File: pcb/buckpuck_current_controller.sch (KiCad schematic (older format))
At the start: 10 parts, among them K1 CCB, P1 POWER, SW1 SPST

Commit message: Added some components to the schematic
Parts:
- added BP? (x3): BUCKPUCK, symbol BUCKPUCK
- added P? (x4): CONN_2, symbol CONN_2
- added RV? (x3): 5k, symbol POT
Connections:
- net labels added: CtrlA, CtrlB, CtrlC, CtrlD, CurrentSenseA, CurrentSenseB, CurrentSenseC, CurrentSenseD, DisplayRX, DisplayTX, PotentiometerA, PotentiometerB, PotentiometerC, PotentiometerD, PwmA, PwmB, PwmC, PwmD, SwitchA, SwitchB, SwitchC, SwitchD, VCC
- wire segments 23 -> 87
- no-connect marks 0 -> 13
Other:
- moved on the sheet: RV1

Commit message: Added single_buckpuck_channel.sch and some datasheets
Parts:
- removed BP1, BP? (x3): BUCKPUCK, symbol BUCKPUCK
- removed K1: CCB, symbol CONN_3
- removed P? (x4): CONN_2, symbol CONN_2
- removed RV1, RV? (x3): 5k, symbol POT
- removed SW1: SPST, symbol SPST
- removed TP1: CS-, symbol TESTPOINT
- removed TP2: CS+, symbol TESTPOINT
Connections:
- net labels added: OnOffSwitchA, OnOffSwitchB, OnOffSwitchC, OnOffSwitchD
- net labels removed: CtrlA, CtrlB, CtrlC, CtrlD, SwitchA, SwitchB, SwitchC, SwitchD, VCC
- wire segments 87 -> 43
- no-connect marks 13 -> 9

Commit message: Finished schematic design, added new datasheets...
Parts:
- added C?: 0.33uF, symbol C
- added C?: 0.1uF, symbol C
- added C? (x2): 10uF, symbol C
- added P?: CONN_2X2, symbol CONN_2X2
- added P?: Display, symbol CONN_4
- added R?: 68, symbol R
- added SW?: SetSwitch, symbol SPST
- added U?: V7809, symbol V7809
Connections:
- net labels added: +5V, RST, VDD
- wire segments 43 -> 89
- no-connect marks 9 -> 8
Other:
- moved on the sheet: U?

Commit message: Finished netlist, begun laying out board.  Added datasheets.
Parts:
- removed SW?: SetSwitch, symbol SPST
- added P3: SetSwitch, symbol CONN_2
- P2: renamed from P?; value CONN_2X2 -> ResetOverride
- gave numbers to parts that had none: 8
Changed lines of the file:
@@
-EESchema Schematic File Version 2  date Tue 17 May 2011 05:19:53 PM PDT
+EESchema Schematic File Version 2  date Wed 18 May 2011 04:50:05 PM PDT
 LIBS:power
 LIBS:device
@@
 Comment4 ""
 $EndDescr
-Connection ~ 6150 1800
-Wire Wire Line
-	6150 1600 6150 1800
+Wire Wire Line
+	2250 5900 2250 6400
 Connection ~ 4250 1800
 Wire Wire Line
-	4250 1900 4250 1800
+	4250 1800 4250 1900
 Wire Wire Line
 	4250 2300 4250 2450
@@
 Connection ~ 3700 1800
 Wire Wire Line
-	4600 1800 3350 1800
+	3350 1800 4600 1800
 Connection ~ 5450 3900
 Wire Wire Line
@@
 	4450 2950 4450 3600
 Wire Wire Line
-	2250 6200 2250 6400
-Wire Wire Line
 	4300 6100 3800 6100
 Wire Wire Line
@@
 	1650 2900 3450 2900
 Wire Wire Line
-	3450 1500 3450 1900
+	3450 1900 3450 1500
 Wire Wire Line
 	1350 1800 1350 950
@@
 Connection ~ 6600 2950
 Wire Wire Line
-	4600 3600 4600 3800
+	4600 3800 4600 3600
 Connection ~ 4600 3700
 Wire Wire Line
@@
 	4300 6200 3800 6200
 Wire Wire Line
-	2650 5000 2250 5000
-Wire Wire Line
-	2250 5000 2250 5200
-Wire Wire Line
-	5450 3900 5450 3700
+	5450 3700 5450 3900
 Wire Wire Line
 	5750 3250 5750 3400
@@
 	5000 2100 5000 2250
 Wire Wire Line
-	5750 1900 5750 1800
+	5750 1800 5750 1900
 Connection ~ 5750 1800
 Wire Wire Line
@@
 Wire Wire Line
 	6550 1800 6550 1650
-$Comp
-L PWR_FLAG #FLG?
-U 1 1 4DD30F98
-P 6150 1600
-F 0 "#FLG?" H 6150 1870 30  0001 C CNN
-F 1 "PWR_FLAG" H 6150 1830 30  0000 C CNN
-	1    6150 1600
-	1    0    0    -1
-$EndComp
-$Comp
-L VDD #PWR?
+Wire Wire Line
+	2650 5000 2050 5000
+Wire Wire Line
+	2050 5000 2050 5700
+Wire Wire Line
+	2050 5700 2250 5700
+$Comp
+L CONN_2 P3
+U 1 1 4DD40675
+P 2600 5800
+F 0 "P3" V 2550 5800 40  0000 C CNN
+F 1 "SetSwitch" V 2650 5800 40  0000 C CNN
+	1    2600 5800
+	1    0    0    -1
+$EndComp
+$Comp
+L VDD #PWR01
 U 1 1 4DD30F8E
 P 6550 1650
-F 0 "#PWR?" H 6550 1750 30  0001 C CNN
+F 0 "#PWR01" H 6550 1750 30  0001 C CNN
 F 1 "VDD" H 6550 1760 30  0000 C CNN
 	1    6550 1650
@@
 $EndComp
 $Comp
-L GND #PWR?
+L GND #PWR02
 U 1 1 4DD30F78
 P 5750 2450
-F 0 "#PWR?" H 5750 2450 30  0001 C CNN
+F 0 "#PWR02" H 5750 2450 30  0001 C CNN
 F 1 "GND" H 5750 2380 30  0001 C CNN
 	1    5750 2450
@@
 $EndComp
 $Comp
-L GND #PWR?
+L GND #PWR03
 U 1 1 4DD30F74
 P 4250 2450
-F 0 "#PWR?" H 4250 2450 30  0001 C CNN
+F 0 "#PWR03" H 4250 2450 30  0001 C CNN
 F 1 "GND" H 4250 2380 30  0001 C CNN
 	1    4250 2450
@@
 $EndComp
 $Comp
-L C C?
+L C C3
 U 1 1 4DD30F54
 P 5750 2100
-F 0 "C?" H 5800 2200 50  0000 L CNN
+F 0 "C3" H 5800 2200 50  0000 L CNN
 F 1 "10uF" H 5800 2000 50  0000 L CNN
 	1    5750 2100
@@
 $EndComp
 $Comp
-L C C?
+L C C2
 U 1 1 4DD30F51
 P 4250 2100
-F 0 "C?" H 4300 2200 50  0000 L CNN
+F 0 "C2" H 4300 2200 50  0000 L CNN
 F 1 "10uF" H 4300 2000 50  0000 L CNN
 	1    4250 2100
@@
 $EndComp
 $Comp
-L GND #PWR?
+L GND #PWR04
 U 1 1 4DD30F46
 P 5000 2250
-F 0 "#PWR?" H 5000 2250 30  0001 C CNN
+F 0 "#PWR04" H 5000 2250 30  0001 C CNN
 F 1 "GND" H 5000 2180 30  0001 C CNN
 	1    5000 2250
@@
 $EndComp
 $Comp
-L V7809 U?
+L V7809 U1
 U 1 1 4DD30F0E
 P 5000 1850
-F 0 "U?" H 5150 1654 60  0000 C CNN
+F 0 "U1" H 5150 1654 60  0000 C CNN
 F 1 "V7809" H 5000 2050 60  0000 C CNN
 	1    5000 1850
@@
 $EndComp
 $Comp
-L +5V #PWR?
+L +5V #PWR05
 U 1 1 4DD308A2
 P 5750 3250
-F 0 "#PWR?" H 5750 3340 20  0001 C CNN
+F 0 "#PWR05" H 5750 3340 20  0001 C CNN
 F 1 "+5V" H 5750 3340 30  0000 C CNN
 	1    5750 3250
@@
 $EndComp
 $Comp
-L PWR_FLAG #FLG?
+L PWR_FLAG #FLG06
 U 1 1 4DD3088D
 P 5700 3850
-F 0 "#FLG?" H 5700 4120 30  0001 C CNN
+F 0 "#FLG06" H 5700 4120 30  0001 C CNN
 F 1 "PWR_FLAG" H 5700 4080 30  0000 C CNN
 	1    5700 3850
@@
 $EndComp
 $Comp
-L +5V #PWR?
+L +5V #PWR07
 U 1 1 4DD3087D
 P 5450 3700
-F 0 "#PWR?" H 5450 3790 20  0001 C CNN
+F 0 "#PWR07" H 5450 3790 20  0001 C CNN
 F 1 "+5V" H 5450 3790 30  0000 C CNN
 	1    5450 3700
@@
 $EndComp
 $Comp
-L VDD #PWR?
+L VDD #PWR08
 U 1 1 4DD3074D
 P 4450 2950
-F 0 "#PWR?" H 4450 3050 30  0001 C CNN
+F 0 "#PWR08" H 4450 3050 30  0001 C CNN
 F 1 "VDD" H 4450 3060 30  0000 C CNN
 	1    4450 2950
@@
 $EndComp
 $Comp
-L GND #PWR?
+L GND #PWR09
 U 1 1 4DD2FA71
 P 2250 6400
-F 0 "#PWR?" H 2250 6400 30  0001 C CNN
+F 0 "#PWR09" H 2250 6400 30  0001 C CNN
 F 1 "GND" H 2250 6330 30  0001 C CNN
 	1    2250 6400
 	1    0    0    -1
-$EndComp
-$Comp
-L SPST SW?
-U 1 1 4DD2FA66
-P 2250 5700
-F 0 "SW?" H 2250 5800 70  0000 C CNN
-F 1 "SetSwitch" H 2250 5600 70  0000 C CNN
-	1    2250 5700
-	0    1    1    0
 $EndComp
 Text Label 3800 6200 0    60   ~ 0
@@
 DisplayRX
 $Comp
-L GND #PWR?
+L GND #PWR010
 U 1 1 4DD2F8D7
 P 3550 6350
-F 0 "#PWR?" H 3550 6350 30  0001 C CNN
+F 0 "#PWR010" H 3550 6350 30  0001 C CNN
 F 1 "GND" H 3550 6280 30  0001 C CNN
 	1    3550 6350
@@
 $EndComp
 $Comp
-L VDD #PWR?
+L VDD #PWR011
 U 1 1 4DD2F8C8
 P 4100 5750
-F 0 "#PWR?" H 4100 5850 30  0001 C CNN
+F 0 "#PWR011" H 4100 5850 30  0001 C CNN
 F 1 "VDD" H 4100 5860 30  0000 C CNN
 	1    4100 5750
@@
 $EndComp
 $Comp
-L CONN_4 P?
+L CONN_4 P4
 U 1 1 4DD2F842
 P 4650 6050
-F 0 "P?" V 4600 6050 50  0000 C CNN
+F 0 "P4" V 4600 6050 50  0000 C CNN
 F 1 "Display" V 4700 6050 50  0000 C CNN
 	1    4650 6050
@@
 $EndComp
 $Comp
-L C C?
+L C C5
 U 1 1 4DD2F791
 P 4600 3400
-F 0 "C?" H 4650 3500 50  0000 L CNN
+F 0 "C5" H 4650 3500 50  0000 L CNN
 F 1 "0.1uF" H 4650 3300 50  0000 L CNN
 	1    4600 3400
@@
 $EndComp
 $Comp
-L GND #PWR?
+L GND #PWR012
 U 1 1 4DD2F728
 P 4600 3800
-F 0 "#PWR?" H 4600 3800 30  0001 C CNN
+F 0 "#PWR012" H 4600 3800 30  0001 C CNN
 F 1 "GND" H 4600 3730 30  0001 C CNN
 	1    4600 3800
@@
 $EndComp
 $Comp
-L GND #PWR?
+L GND #PWR013
 U 1 1 4DD2F63F
 P 6800 3600
-F 0 "#PWR?" H 6800 3600 30  0001 C CNN
+F 0 "#PWR013" H 6800 3600 30  0001 C CNN
 F 1 "GND" H 6800 3530 30  0001 C CNN
 	1    6800 3600
@@
 $EndComp
 $Comp
-L R R?
+L R R1
 U 1 1 4DD2F567
 P 6150 3400
-F 0 "R?" V 6230 3400 50  0000 C CNN
+F 0 "R1" V 6230 3400 50  0000 C CNN
 F 1 "68" V 6150 3400 50  0000 C CNN
 	1    6150 3400
@@
 $EndComp
 $Comp
-L C C?
+L C C4
 U 1 1 4DD2F558
 P 6800 3250
-F 0 "C?" H 6850 3350 50  0000 L CNN
+F 0 "C4" H 6850 3350 50  0000 L CNN
 F 1 "0.33uF" H 6850 3150 50  0000 L CNN
 	1    6800 3250
@@
 NoConn ~ 5650 3050
 $Comp
-L CONN_2X2 P?
+L CONN_2X2 P2
 U 1 1 4DD2F1DB
 P 6050 3000
-F 0 "P?" H 6050 3150 50  0000 C CNN
-F 1 "CONN_2X2" H 6060 2870 40  0000 C CNN
+F 0 "P2" H 6050 3150 50  0000 C CNN
+F 1 "ResetOverride" H 6060 2870 40  0000 C CNN
 	1    6050 3000
 	1    0    0    -1
@@
 DisplayRX
 $Comp
-L GND #PWR01
+L GND #PWR014
 U 1 1 4DB0D0E3
 P 1550 4000
-F 0 "#PWR01" H 1550 4000 30  0001 C CNN
+F 0 "#PWR014" H 1550 4000 30  0001 C CNN
 F 1 "GND" H 1550 3930 30  0001 C CNN
 	1    1550 4000
@@
 CurrentSenseA
 $Comp
-L VAA #PWR?
+L VAA #PWR1
 U 1 1 4DAF3EF4
 P 3700 1600
-F 0 "#PWR?" H 3700 1660 30  0001 C CNN
+F 0 "#PWR1" H 3700 1660 30  0001 C CNN
 F 1 "VAA" H 3700 1710 30  0000 C CNN
 	1    3700 1600
@@
 $EndComp
 $Comp
-L ARDUINO_NANO U?
+L ARDUINO_NANO U2
 U 1 1 4DAF2A1C
 P 3500 4350
-F 0 "U?" H 3050 5300 60  0000 C CNN
+F 0 "U2" H 3050 5300 60  0000 C CNN
 F 1 "ARDUINO_NANO" H 3500 3500 60  0000 C CNN
 	1    3500 4350
@@
 $EndComp
 $Comp
-L GND #PWR02
+L GND #PWR015
 U 1 1 4B884901
 P 3200 3050
-F 0 "#PWR02" H 3200 3050 30  0001 C CNN
+F 0 "#PWR015" H 3200 3050 30  0001 C CNN
 F 1 "GND" H 3200 2980 30  0001 C CNN
 	1    3200 3050
@@
 $EndComp
 $Comp
-L PWR_FLAG #FLG03
+L PWR_FLAG #FLG016
 U 1 1 4B61DEC3
 P 2950 2750
-F 0 "#FLG03" H 2950 3020 30  0001 C CNN
+F 0 "#FLG016" H 2950 3020 30  0001 C CNN
 F 1 "PWR_FLAG" H 2950 2980 30  0000 C CNN
 	1    2950 2750
@@
 $EndComp
 $Comp
-L PWR_FLAG #FLG04
+L PWR_FLAG #FLG017
 U 1 1 4B61DEA9
 P 2400 750
-F 0 "#FLG04" H 2400 1020 30  0001 C CNN
+F 0 "#FLG017" H 2400 1020 30  0001 C CNN
 F 1 "PWR_FLAG" H 2400 980 30  0000 C CNN
 	1    2400 750
@@
 $EndComp
 $Comp
-L PWR_FLAG #FLG05
+L PWR_FLAG #FLG018
 U 1 1 4B61DE8F
 P 3450 1500
-F 0 "#FLG05" H 3450 1770 30  0001 C CNN
+F 0 "#FLG018" H 3450 1770 30  0001 C CNN
 F 1 "PWR_FLAG" H 3450 1730 30  0000 C CNN
 	1    3450 1500

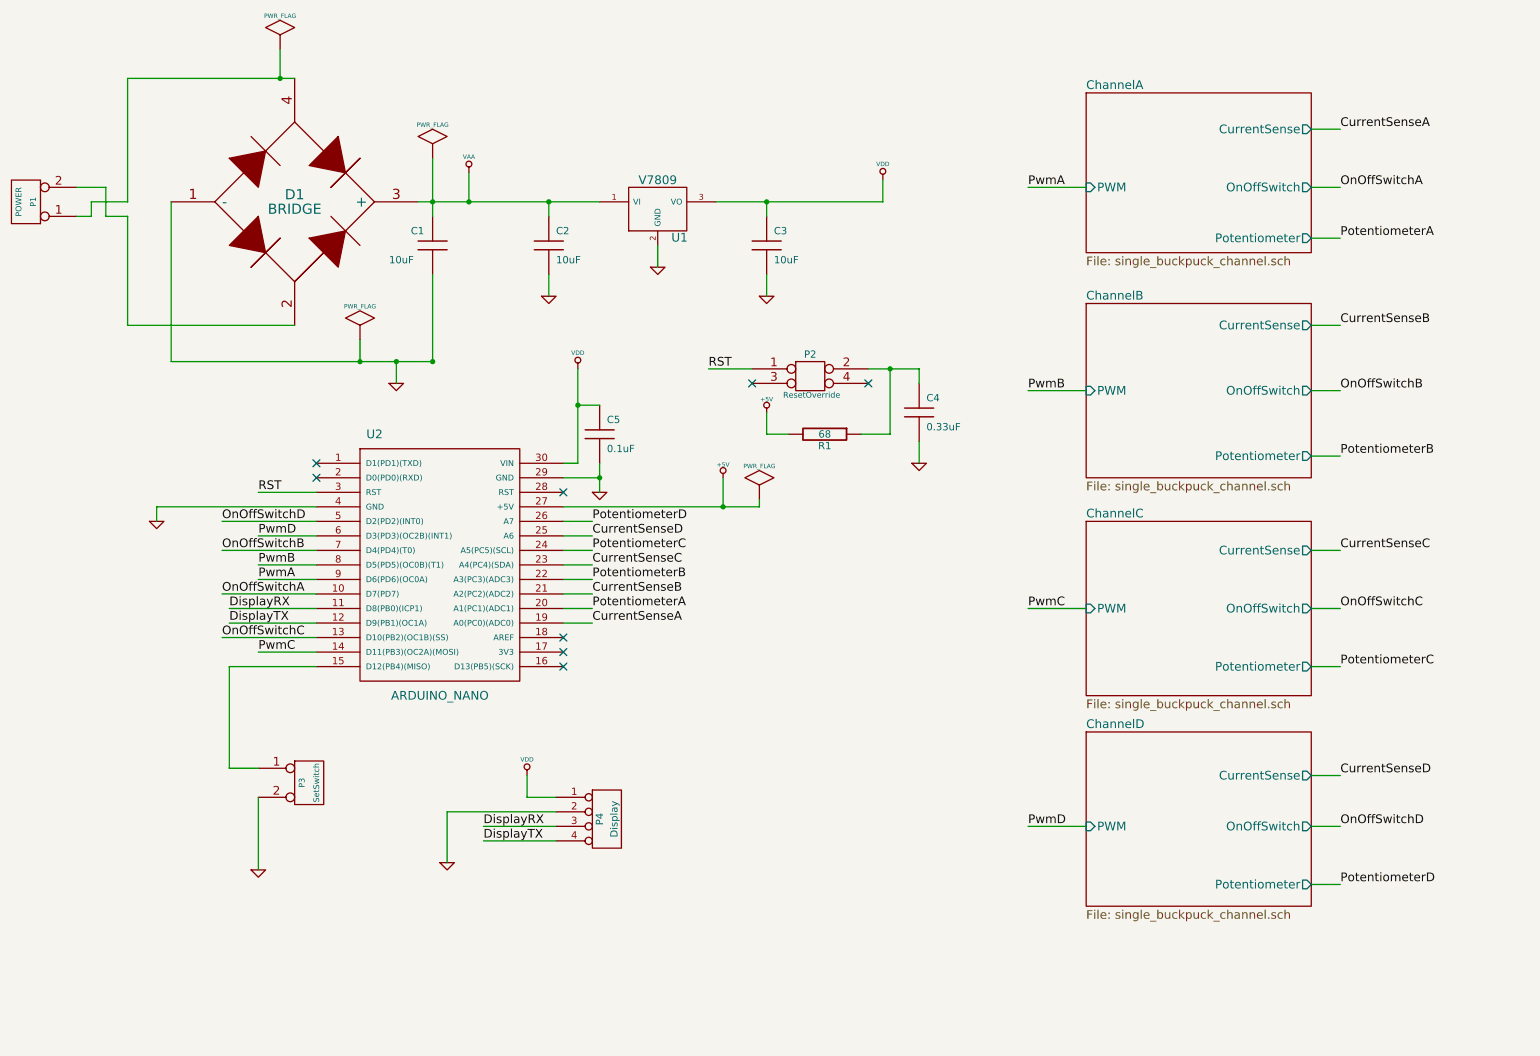
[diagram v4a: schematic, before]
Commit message: Finished routing board.  Examine one more time before being made.
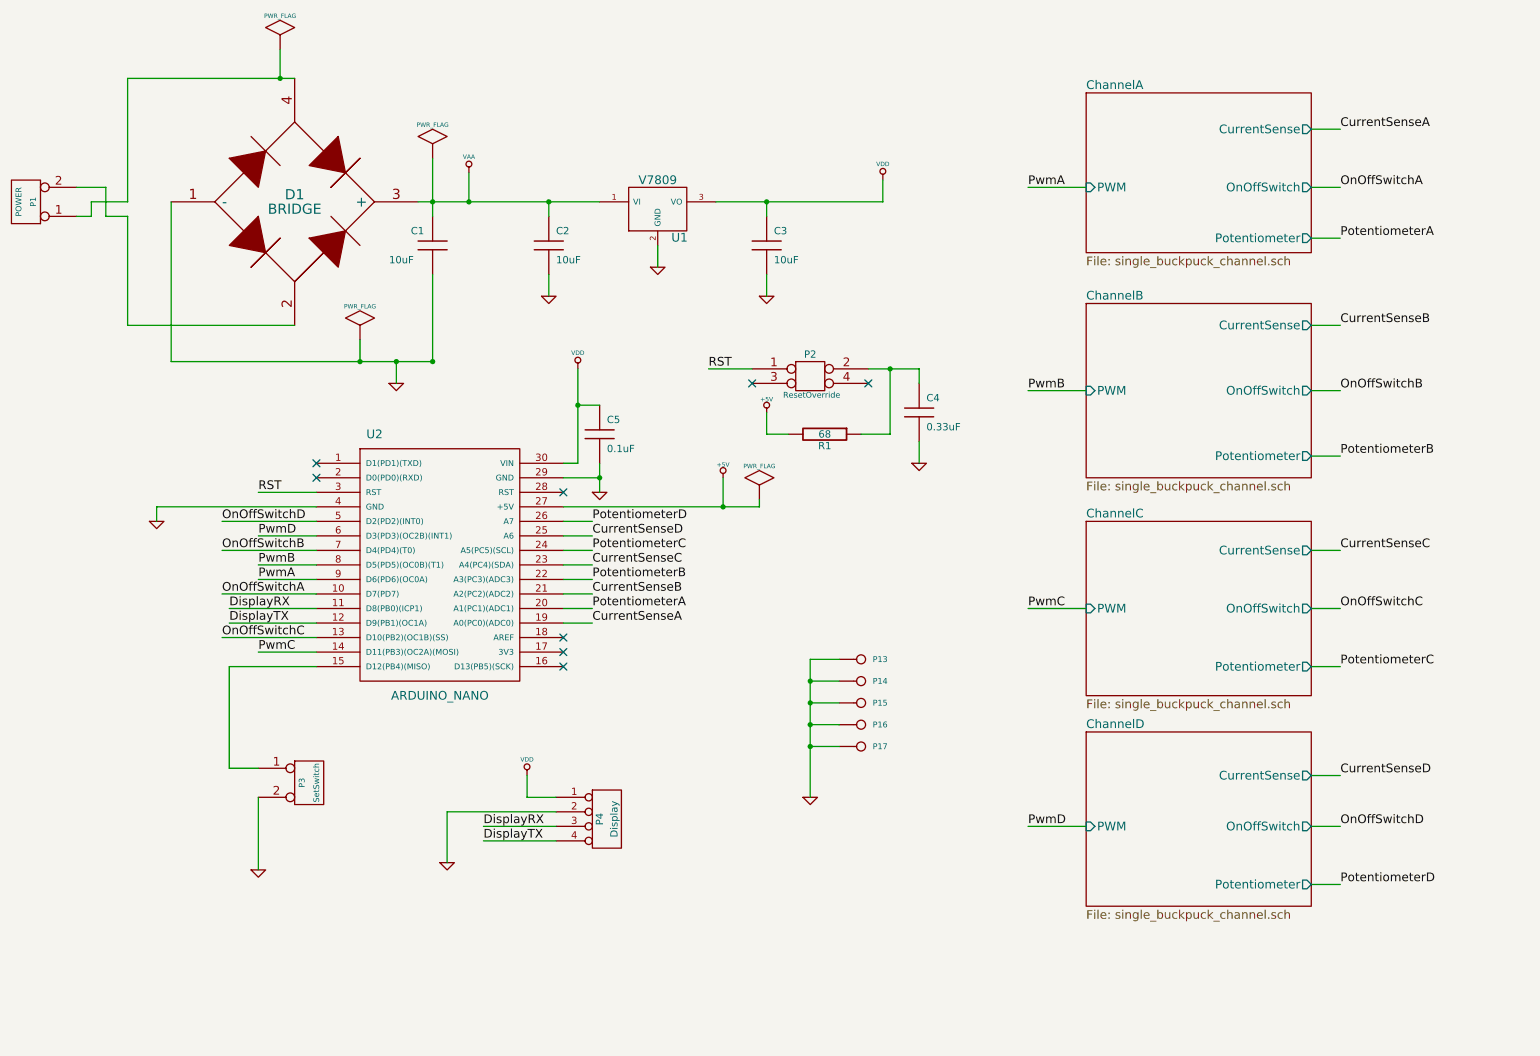
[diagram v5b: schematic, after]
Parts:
- added P13, P14, P15, P16, P17: CONN_1, symbol CONN_1
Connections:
- net GND: now also P13.1, P14.1, P15.1, P16.1, P17.1
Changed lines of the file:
@@
-EESchema Schematic File Version 2  date Wed 18 May 2011 04:50:05 PM PDT
+EESchema Schematic File Version 2  date Fri 20 May 2011 05:25:28 PM PDT
 LIBS:power
 LIBS:device
@@
 Sheet 1 5
 Title "Buckpuck Current Controller"
-Date "18 may 2011"
+Date "21 may 2011"
 Rev "1.0"
 Comp ""
@@
 Comment4 ""
 $EndDescr
+Connection ~ 6050 5400
+Wire Wire Line
+	6050 5400 6250 5400
+Connection ~ 6050 5100
+Wire Wire Line
+	6250 5100 6050 5100
 Wire Wire Line
 	2250 5900 2250 6400
@@
 	3450 1900 3450 1500
 Wire Wire Line
-	1350 1800 1350 950
+	1350 950  1350 1800
 Wire Wire Line
 	1350 1800 1100 1800
@@
 	1350 2650 1350 1900
 Wire Wire Line
-	1350 950  2500 950
+	2500 950  1350 950
 Wire Wire Line
 	3450 2900 3450 2300
@@
 Wire Wire Line
 	2050 5700 2250 5700
+Wire Wire Line
+	6050 4950 6250 4950
+Wire Wire Line
+	6050 5900 6050 4950
+Wire Wire Line
+	6250 5250 6050 5250
+Connection ~ 6050 5250
+Wire Wire Line
+	6250 5550 6050 5550
+Connection ~ 6050 5550
+$Comp
+L GND #PWR01
+U 1 1 4DD6F401
+P 6050 5900
+F 0 "#PWR01" H 6050 5900 30  0001 C CNN
+F 1 "GND" H 6050 5830 30  0001 C CNN
+	1    6050 5900
+	1    0    0    -1
+$EndComp
+$Comp
+L CONN_1 P17
+U 1 1 4DD6F3EE
+P 6400 5550
+F 0 "P17" H 6480 5550 40  0000 L CNN
+F 1 "CONN_1" H 6400 5605 30  0001 C CNN
+	1    6400 5550
+	1    0    0    -1
+$EndComp
+$Comp
+L CONN_1 P16
+U 1 1 4DD6F3EB
+P 6400 5400
+F 0 "P16" H 6480 5400 40  0000 L CNN
+F 1 "CONN_1" H 6400 5455 30  0001 C CNN
+	1    6400 5400
+	1    0    0    -1
+$EndComp
+$Comp
+L CONN_1 P15
+U 1 1 4DD6F3E8
+P 6400 5250
+F 0 "P15" H 6480 5250 40  0000 L CNN
+F 1 "CONN_1" H 6400 5305 30  0001 C CNN
+	1    6400 5250
+	1    0    0    -1
+$EndComp
+$Comp
+L CONN_1 P14
+U 1 1 4DD6F3E5
+P 6400 5100
+F 0 "P14" H 6480 5100 40  0000 L CNN
+F 1 "CONN_1" H 6400 5155 30  0001 C CNN
+	1    6400 5100
+	1    0    0    -1
+$EndComp
+$Comp
+L CONN_1 P13
+U 1 1 4DD6F3DD
+P 6400 4950
+F 0 "P13" H 6480 4950 40  0000 L CNN
+F 1 "CONN_1" H 6400 5005 30  0001 C CNN
+	1    6400 4950
+	1    0    0    -1
+$EndComp
 $Comp
 L CONN_2 P3
@@
 $EndComp
 $Comp
-L VDD #PWR01
+L VDD #PWR02
 U 1 1 4DD30F8E
 P 6550 1650
-F 0 "#PWR01" H 6550 1750 30  0001 C CNN
+F 0 "#PWR02" H 6550 1750 30  0001 C CNN
 F 1 "VDD" H 6550 1760 30  0000 C CNN
 	1    6550 1650
@@
 $EndComp
 $Comp
-L GND #PWR02
+L GND #PWR03
 U 1 1 4DD30F78
 P 5750 2450
-F 0 "#PWR02" H 5750 2450 30  0001 C CNN
+F 0 "#PWR03" H 5750 2450 30  0001 C CNN
 F 1 "GND" H 5750 2380 30  0001 C CNN
 	1    5750 2450
@@
 $EndComp
 $Comp
-L GND #PWR03
+L GND #PWR04
 U 1 1 4DD30F74
 P 4250 2450
-F 0 "#PWR03" H 4250 2450 30  0001 C CNN
+F 0 "#PWR04" H 4250 2450 30  0001 C CNN
 F 1 "GND" H 4250 2380 30  0001 C CNN
 	1    4250 2450
@@
 $EndComp
 $Comp
-L GND #PWR04
+L GND #PWR05
 U 1 1 4DD30F46
 P 5000 2250
-F 0 "#PWR04" H 5000 2250 30  0001 C CNN
+F 0 "#PWR05" H 5000 2250 30  0001 C CNN
 F 1 "GND" H 5000 2180 30  0001 C CNN
 	1    5000 2250
@@
 $EndComp
 $Comp
-L +5V #PWR05
+L +5V #PWR06
 U 1 1 4DD308A2
 P 5750 3250
-F 0 "#PWR05" H 5750 3340 20  0001 C CNN
+F 0 "#PWR06" H 5750 3340 20  0001 C CNN
 F 1 "+5V" H 5750 3340 30  0000 C CNN
 	1    5750 3250
@@
 $EndComp
 $Comp
-L PWR_FLAG #FLG06
+L PWR_FLAG #FLG07
 U 1 1 4DD3088D
 P 5700 3850
-F 0 "#FLG06" H 5700 4120 30  0001 C CNN
+F 0 "#FLG07" H 5700 4120 30  0001 C CNN
 F 1 "PWR_FLAG" H 5700 4080 30  0000 C CNN
 	1    5700 3850
@@
 $EndComp
 $Comp
-L +5V #PWR07
+L +5V #PWR08
 U 1 1 4DD3087D
 P 5450 3700
-F 0 "#PWR07" H 5450 3790 20  0001 C CNN
+F 0 "#PWR08" H 5450 3790 20  0001 C CNN
 F 1 "+5V" H 5450 3790 30  0000 C CNN
 	1    5450 3700
@@
 $EndComp
 $Comp
-L VDD #PWR08
+L VDD #PWR09
 U 1 1 4DD3074D
 P 4450 2950
-F 0 "#PWR08" H 4450 3050 30  0001 C CNN
+F 0 "#PWR09" H 4450 3050 30  0001 C CNN
 F 1 "VDD" H 4450 3060 30  0000 C CNN
 	1    4450 2950
@@
 $EndComp
 $Comp
-L GND #PWR09
+L GND #PWR010
 U 1 1 4DD2FA71
 P 2250 6400
-F 0 "#PWR09" H 2250 6400 30  0001 C CNN
+F 0 "#PWR010" H 2250 6400 30  0001 C CNN
 F 1 "GND" H 2250 6330 30  0001 C CNN
 	1    2250 6400
@@
 DisplayRX
 $Comp
-L GND #PWR010
+L GND #PWR011
 U 1 1 4DD2F8D7
 P 3550 6350
-F 0 "#PWR010" H 3550 6350 30  0001 C CNN
+F 0 "#PWR011" H 3550 6350 30  0001 C CNN
 F 1 "GND" H 3550 6280 30  0001 C CNN
 	1    3550 6350
@@
 $EndComp
 $Comp
-L VDD #PWR011
+L VDD #PWR012
 U 1 1 4DD2F8C8
 P 4100 5750
-F 0 "#PWR011" H 4100 5850 30  0001 C CNN
+F 0 "#PWR012" H 4100 5850 30  0001 C CNN
 F 1 "VDD" H 4100 5860 30  0000 C CNN
 	1    4100 5750
@@
 $EndComp
 $Comp
-L GND #PWR012
+L GND #PWR013
 U 1 1 4DD2F728
 P 4600 3800
-F 0 "#PWR012" H 4600 3800 30  0001 C CNN
+F 0 "#PWR013" H 4600 3800 30  0001 C CNN
 F 1 "GND" H 4600 3730 30  0001 C CNN
 	1    4600 3800
@@
 $EndComp
 $Comp
-L GND #PWR013
+L GND #PWR014
 U 1 1 4DD2F63F
 P 6800 3600
-F 0 "#PWR013" H 6800 3600 30  0001 C CNN
+F 0 "#PWR014" H 6800 3600 30  0001 C CNN
 F 1 "GND" H 6800 3530 30  0001 C CNN
 	1    6800 3600
@@
 DisplayRX
 $Comp
-L GND #PWR014
+L GND #PWR015
 U 1 1 4DB0D0E3
 P 1550 4000
-F 0 "#PWR014" H 1550 4000 30  0001 C CNN
+F 0 "#PWR015" H 1550 4000 30  0001 C CNN
 F 1 "GND" H 1550 3930 30  0001 C CNN
 	1    1550 4000
@@
 $EndComp
 $Comp
-L GND #PWR015
+L GND #PWR016
 U 1 1 4B884901
 P 3200 3050
-F 0 "#PWR015" H 3200 3050 30  0001 C CNN
+F 0 "#PWR016" H 3200 3050 30  0001 C CNN
 F 1 "GND" H 3200 2980 30  0001 C CNN
 	1    3200 3050
@@
 $EndComp
 $Comp
-L PWR_FLAG #FLG016
+L PWR_FLAG #FLG017
 U 1 1 4B61DEC3
 P 2950 2750
-F 0 "#FLG016" H 2950 3020 30  0001 C CNN
+F 0 "#FLG017" H 2950 3020 30  0001 C CNN
 F 1 "PWR_FLAG" H 2950 2980 30  0000 C CNN
 	1    2950 2750
@@
 $EndComp
 $Comp
-L PWR_FLAG #FLG017
+L PWR_FLAG #FLG018
 U 1 1 4B61DEA9
 P 2400 750
-F 0 "#FLG017" H 2400 1020 30  0001 C CNN
+F 0 "#FLG018" H 2400 1020 30  0001 C CNN
 F 1 "PWR_FLAG" H 2400 980 30  0000 C CNN
 	1    2400 750
@@
 $EndComp
 $Comp
-L PWR_FLAG #FLG018
+L PWR_FLAG #FLG019
 U 1 1 4B61DE8F
 P 3450 1500
-F 0 "#FLG018" H 3450 1770 30  0001 C CNN
+F 0 "#FLG019" H 3450 1770 30  0001 C CNN
 F 1 "PWR_FLAG" H 3450 1730 30  0000 C CNN
 	1    3450 1500
